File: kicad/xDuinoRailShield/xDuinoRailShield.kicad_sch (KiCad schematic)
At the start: 0 parts

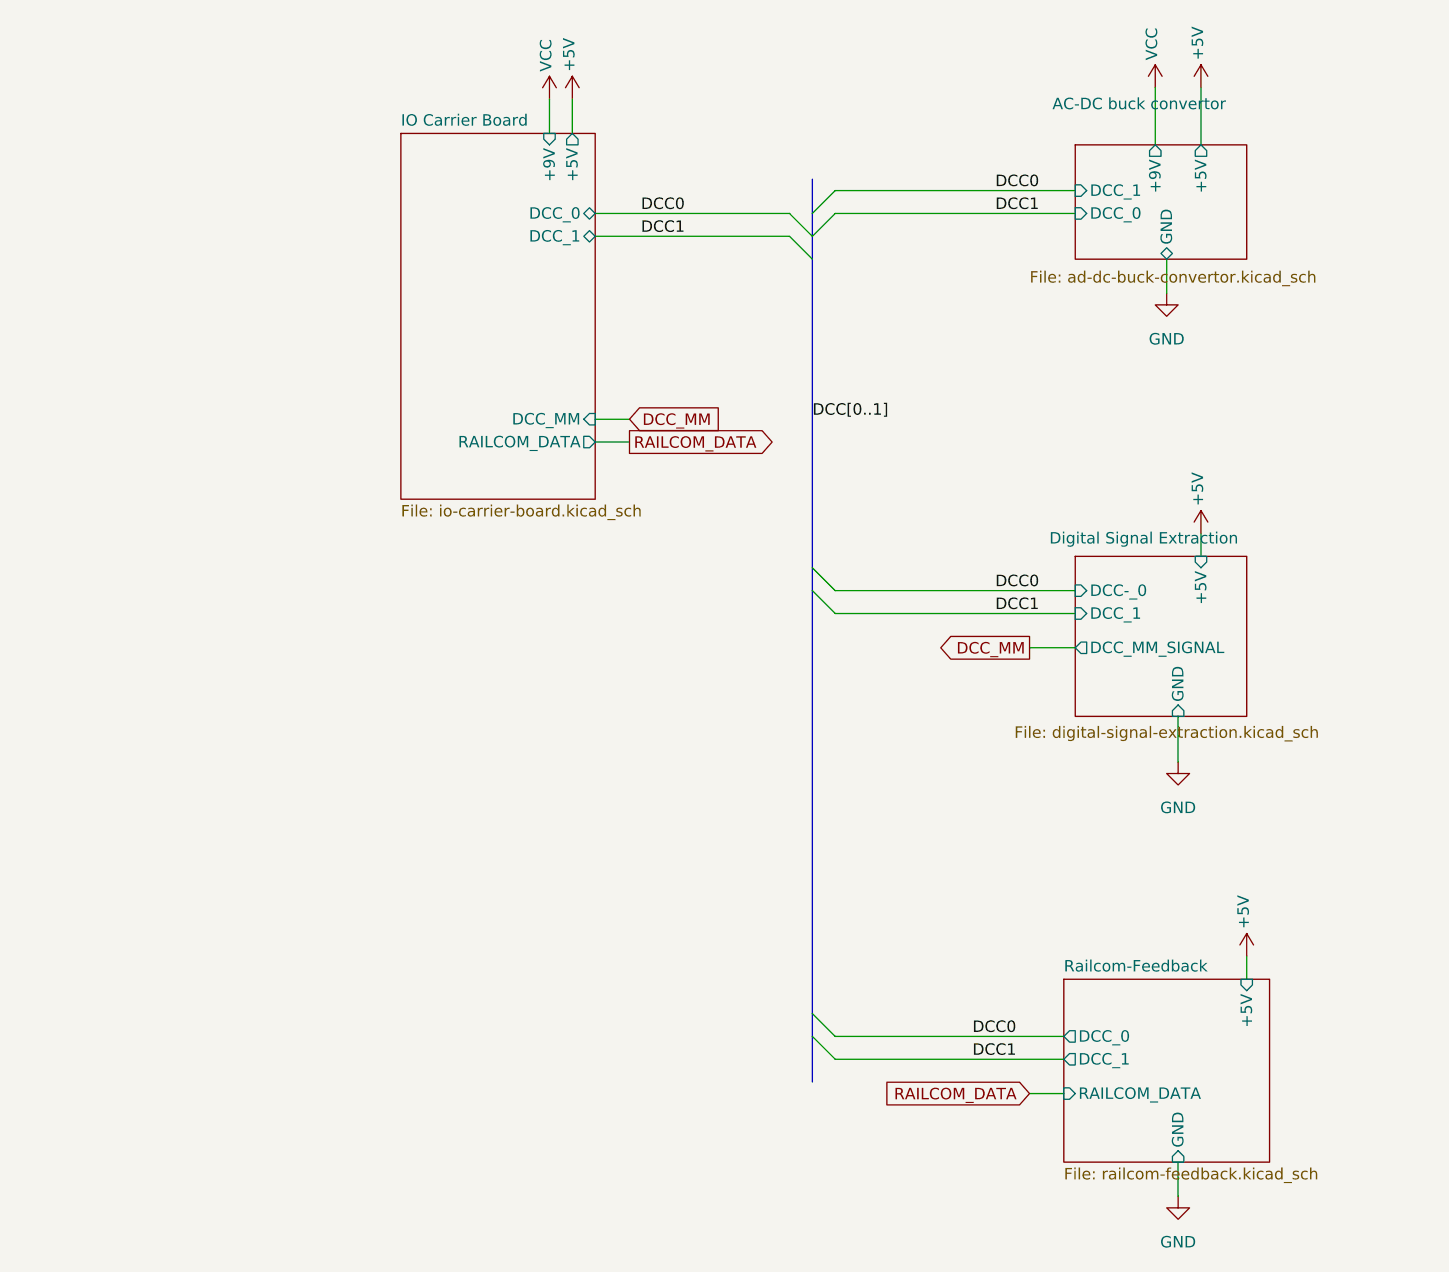
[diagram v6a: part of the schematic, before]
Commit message: Add Analog signal extraction draft
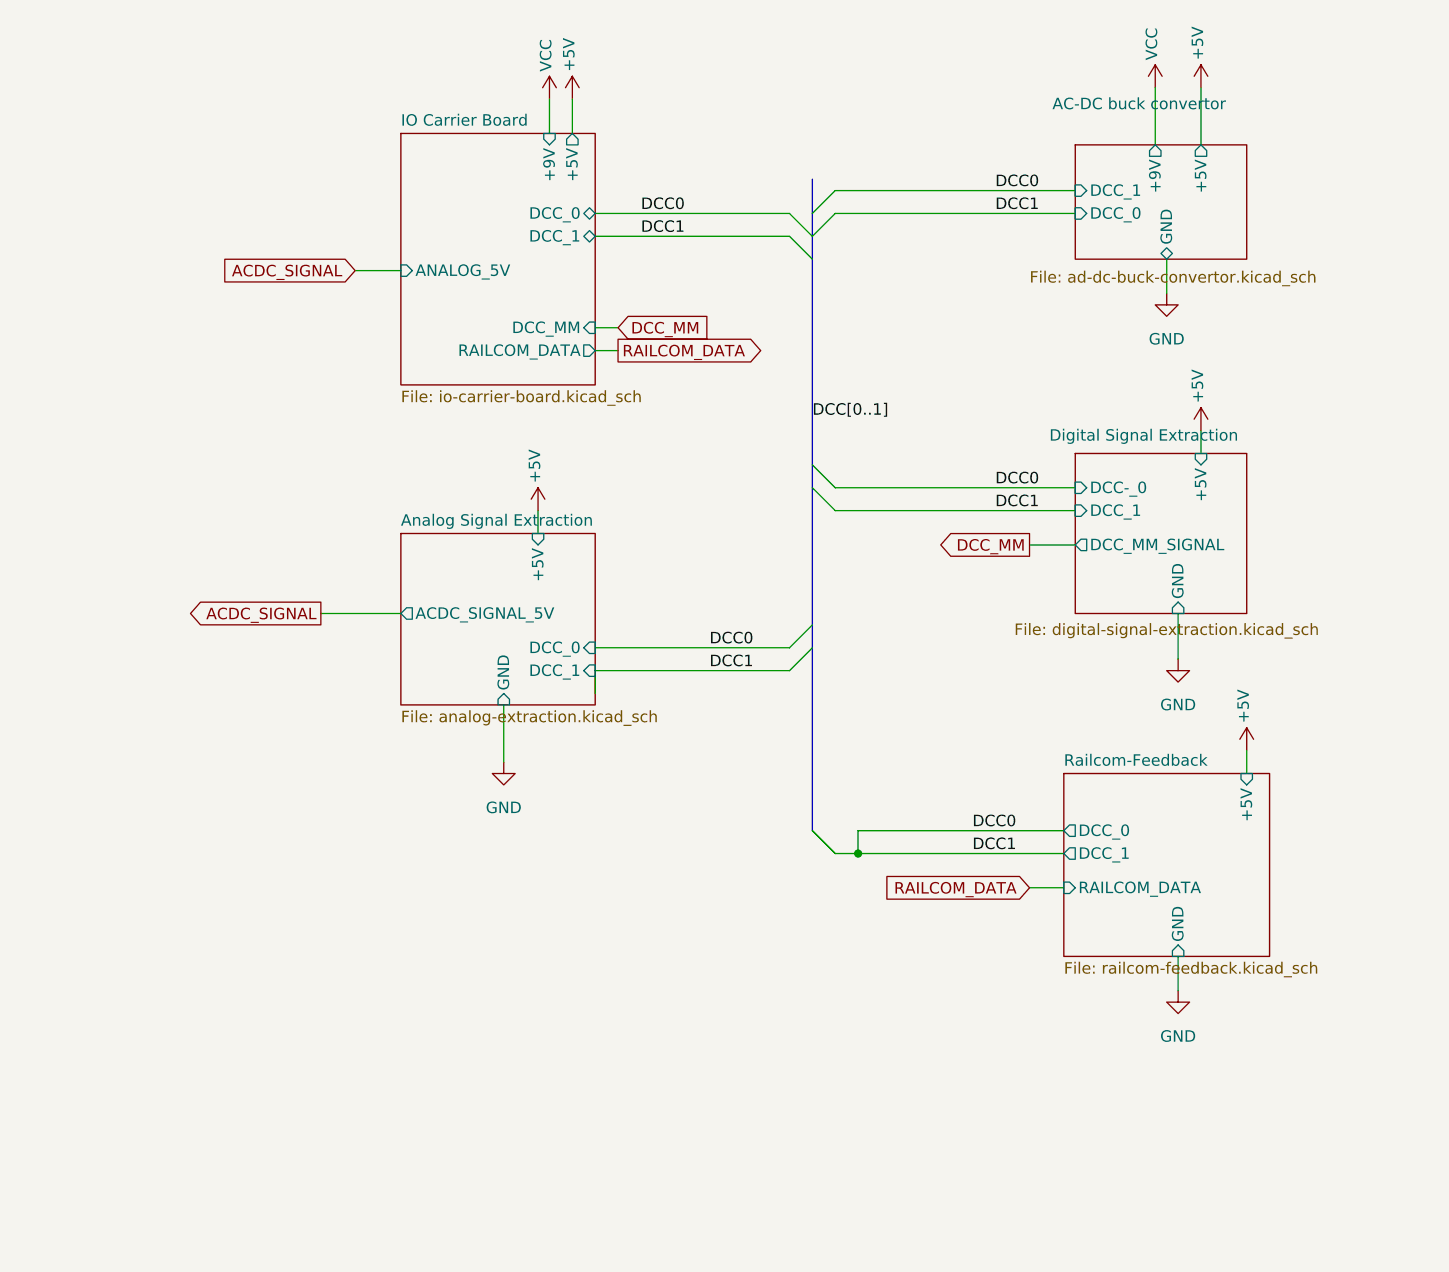
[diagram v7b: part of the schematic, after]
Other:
- added sheet Analog Signal Extraction (analog-extraction.kicad_sch)
- sheet IO Carrier Board ports: added ANALOG_5V; removed none

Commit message: xXiaoCentralMini
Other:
- sheet AC-DC buck convertor renamed AC-DC power supply
- sheet IO Carrier Board renamed MCU Carrier Board
- added sheet Audio Jack 3.5mm (audio_jack.kicad_sch)
- added sheet Loco Adapters (loco-adapters.kicad_sch)
- sheet MCU Carrier Board ports: added DAC, GND; removed none
